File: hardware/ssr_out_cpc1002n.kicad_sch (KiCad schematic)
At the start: 2 parts, among them U6 CPC1002N

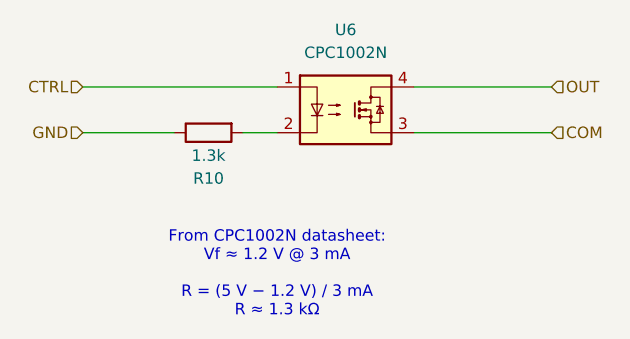
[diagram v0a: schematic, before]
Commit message: chore(hw): migrate KiCad files to the KiCad 10 format
Via `kicad-cli sch upgrade` / `pcb upgrade` (bread-infra
scripts/upgrade_kicad10.sh). Verified lossless: identical netlist, footprint
positions and routing.

Note `sch upgrade` does not cascade into hierarchical sub-sheets, so every
.kicad_sch is upgraded individually -- upgrading only the root sheet leaves
sub-sheets on the old format, which looks migrated and is not.
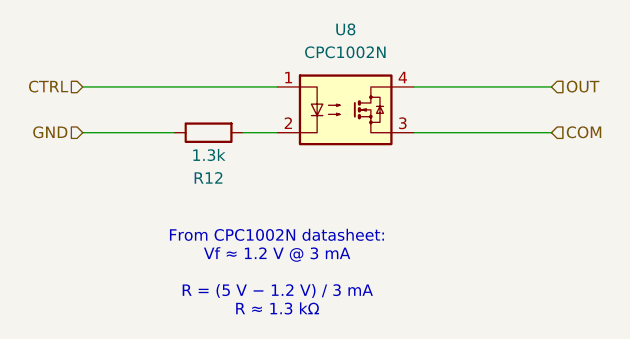
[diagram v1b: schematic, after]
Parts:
- renumbered R10 to R12, U6 to U8
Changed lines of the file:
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@@
 (kicad_sch
-	(version 20250114)
+	(version 20260306)
 	(generator "eeschema")
-	(generator_version "9.0")
+	(generator_version "10.0")
 	(paper "A4")
 	(text "From CPC1002N datasheet: \nVf ≈ 1.2 V @ 3 mA\n\nR = (5 V − 1.2 V) / 3 mA \nR ≈ 1.3 kΩ \n"
@@
 		(mirror x)
 		(unit 1)
+		(body_style 1)
 		(exclude_from_sim no)
 		(in_bom yes)
 		(on_board yes)
+		(in_pos_files yes)
 		(dnp no)
-		(property "Reference" "R10"
+		(property "Reference" "R12"
 			(at 107.95 99.06 90)
+			(show_name no)
+			(do_not_autoplace no)
 			(effects
 				(font
@@
 		(property "Value" "1.3k"
 			(at 107.95 96.52 90)
+			(show_name no)
+			(do_not_autoplace no)
 			(effects
 				(font
@@
 		(property "Footprint" "Resistor_SMD:R_0603_1608Metric"
 			(at 107.95 92.202 90)
-			(effects
-				(font
-					(size 1.27 1.27)
-				)
-				(hide yes)
-			)
-		)
-		(property "Datasheet" "~"
+			(hide yes)
+			(show_name no)
+			(do_not_autoplace no)
+			(effects
+				(font
+					(size 1.27 1.27)
+				)
+			)
+		)
+		(property "Datasheet" ""
 			(at 107.95 93.98 0)
-			(effects
-				(font
-					(size 1.27 1.27)
-				)
-				(hide yes)
+			(hide yes)
+			(show_name no)
+			(do_not_autoplace no)
+			(effects
+				(font
+					(size 1.27 1.27)
+				)
 			)
 		)
 		(property "Description" "Resistor"
 			(at 107.95 93.98 0)
-			(effects
-				(font
-					(size 1.27 1.27)
-				)
-				(hide yes)
+			(hide yes)
+			(show_name no)
+			(do_not_autoplace no)
+			(effects
+				(font
+					(size 1.27 1.27)
+				)
 			)
 		)
@@
 		(at 123.19 91.44 0)
 		(unit 1)
+		(body_style 1)
 		(exclude_from_sim no)
 		(in_bom yes)
 		(on_board yes)
+		(in_pos_files yes)
 		(dnp no)
 		(fields_autoplaced yes)
-		(property "Reference" "U6"
+		(property "Reference" "U8"
 			(at 123.19 82.55 0)
+			(show_name no)
+			(do_not_autoplace no)
 			(effects
 				(font
@@
 		(property "Value" "CPC1002N"
 			(at 123.19 85.09 0)
+			(show_name no)
+			(do_not_autoplace no)
 			(effects
 				(font
@@
 		(property "Footprint" "Package_SO:SOP-4_3.8x4.1mm_P2.54mm"
 			(at 123.19 96.774 0)
+			(hide yes)
+			(show_name no)
+			(do_not_autoplace no)
 			(effects
 				(font
@@
 					(italic yes)
 				)
-				(hide yes)
 			)
 		)
 		(property "Datasheet" "http://www.ixysic.com/home/pdfs.nsf/www/CPC1002N.pdf/$file/CPC1002N.pdf"
 			(at 123.19 100.838 0)
-			(effects
-				(font
-					(size 1.27 1.27)
-				)
-				(hide yes)
+			(hide yes)
+			(show_name no)
+			(do_not_autoplace no)
+			(effects
+				(font
+					(size 1.27 1.27)
+				)
 			)
 		)
 		(property "Description" "Form A, Solid State Relay (Photo MOSFET) 60V, 0.7A, 0.55Ohm, SOP-4"
 			(at 123.19 98.806 0)
-			(effects
-				(font
-					(size 1.27 1.27)
-				)
-				(hide yes)
-			)
-		)
+			(hide yes)
+			(show_name no)
+			(do_not_autoplace no)
+			(effects
+				(font
+					(size 1.27 1.27)
+				)
+			)
+		)
